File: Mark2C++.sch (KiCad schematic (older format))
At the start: 267 parts, among them U1 12AX7, U10 L7812, U11 6P6S, U15 6P6S, U2 12AX7, U3 12AX7, U4 NE5532, U5 NE5532, U6 NE5532, U7 NE5532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

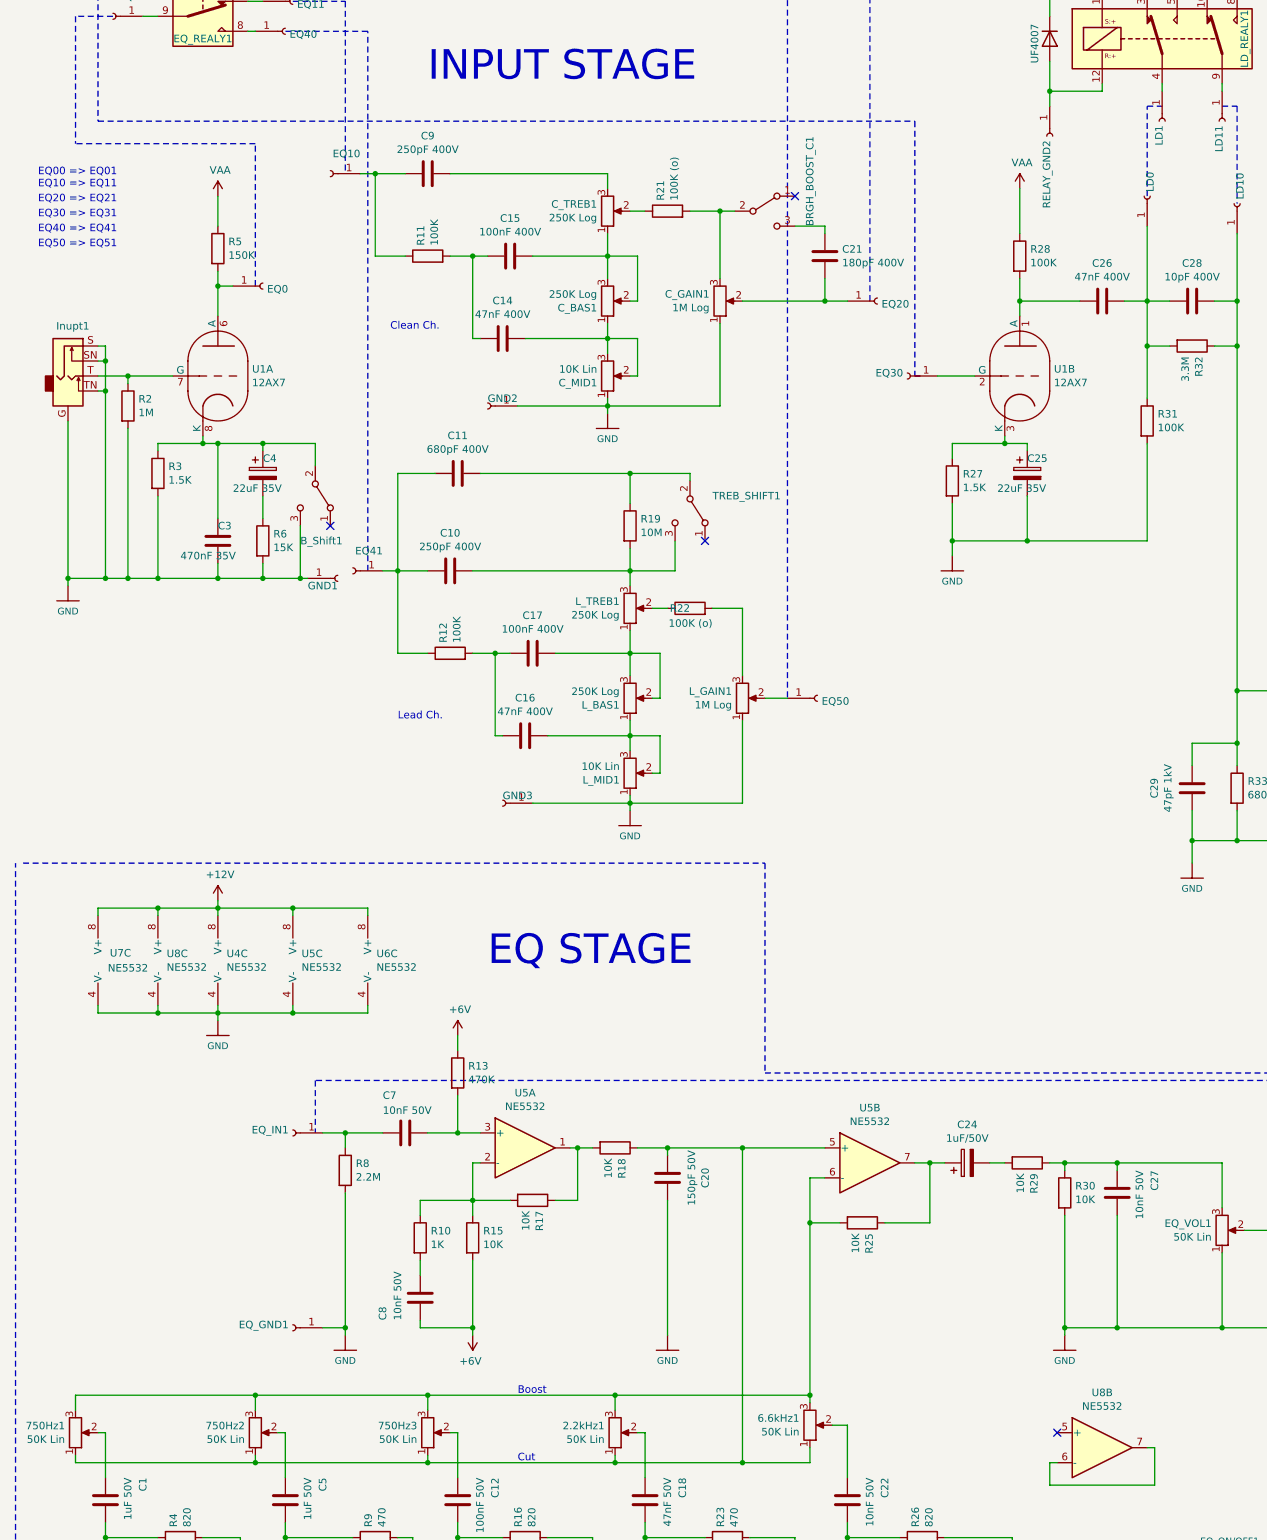
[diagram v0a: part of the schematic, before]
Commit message: small changes
- Poprawki w okolicach sekcji Lead
- Poprawiona nazwa wartości post EQ
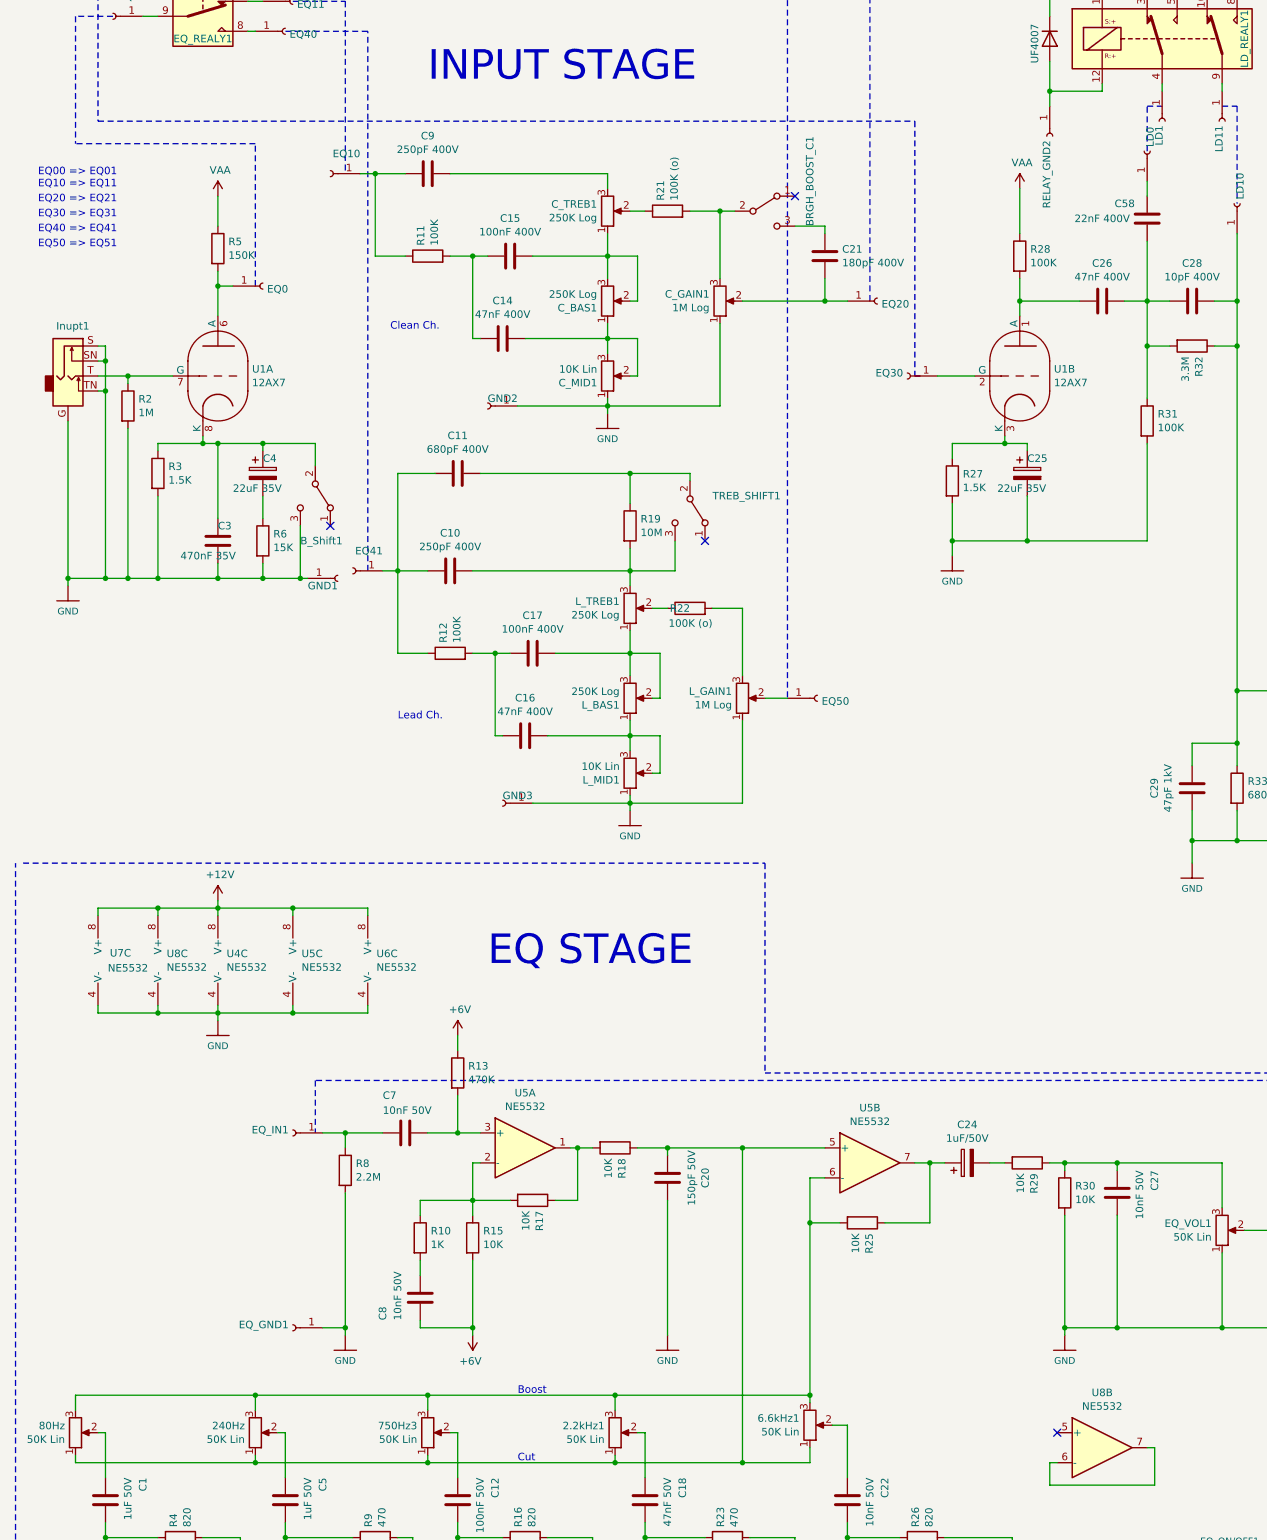
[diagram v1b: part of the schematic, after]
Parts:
- added C58: 22nF 400V, Capacitor_THT:C_Rect_L18.0mm_W6.0mm_P15.00mm_FKS3_FKP3, symbol Device:C
- renumbered 750Hz2 to 240Hz, 750Hz1 to 80Hz
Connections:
- net at C26.1, C28.2, R31.1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: now also C58.2; no longer LD0.1 (Pin_1)
- new net: C58.1, LD0.1 (Pin_1)
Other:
- moved on the sheet: LD0
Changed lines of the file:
@@
 L Connector:Conn_01x01_Female LD0
 U 1 1 64B6227D
-P 8000 3200
-F 0 "LD0" H 8028 3180 50  0000 L CNN
-F 1 "Conn_01x01_Female" H 8028 3135 50  0001 L CNN
-F 2 "Connectors:1X01_2MM" H 8000 3200 50  0001 C CNN
-F 3 "~" H 8000 3200 50  0001 C CNN
-	1    8000 3200
+P 8000 2900
+F 0 "LD0" H 8028 2880 50  0000 L CNN
+F 1 "Conn_01x01_Female" H 8028 2835 50  0001 L CNN
+F 2 "Connectors:1X01_2MM" H 8000 2900 50  0001 C CNN
+F 3 "~" H 8000 2900 50  0001 C CNN
+	1    8000 2900
 	0    -1   -1   0
 $EndComp
 Wire Wire Line
 	7850 3900 8000 3900
-Wire Wire Line
-	8000 3900 8000 3400
 $Comp
 L Device:C C28
@@
 	0    1    1    0
 $EndComp
-Wire Wire Line
-	8150 3900 8000 3900
 Connection ~ 8000 3900
 $Comp
@@
 	8500 2500 8500 2450
 Wire Notes Line rgb(255, 0, 0)
-	8000 3200 8000 2600
-Wire Notes Line rgb(255, 0, 0)
 	8000 2600 8100 2600
 Wire Notes Line rgb(255, 0, 0)
@@
 Connection ~ 2250 12150
 $Comp
-L Device:R_POT 750Hz2
+L Device:R_POT 240Hz
 U 1 1 65F391A3
 P 2050 11450
-F 0 "750Hz2" H 1980 11404 50  0000 R CNN
+F 0 "240Hz" H 1980 11404 50  0000 R CNN
 F 1 "50K Lin" H 1980 11495 50  0000 R CNN
 F 2 "Potentiometer_THT:Potentiometer_Bourns_PTA4543_Single_Slide" H 2050 11450 50  0001 C CNN
@@
 Connection ~ 1050 12850
 $Comp
-L Device:R_POT 750Hz1
+L Device:R_POT 80Hz
 U 1 1 663D8493
 P 850 11450
-F 0 "750Hz1" H 780 11404 50  0000 R CNN
+F 0 "80Hz" H 780 11404 50  0000 R CNN
 F 1 "50K Lin" H 780 11495 50  0000 R CNN
 F 2 "Potentiometer_THT:Potentiometer_Bourns_PTA4543_Single_Slide" H 850 11450 50  0001 C CNN
@@
 	1000 8650 1400 8650
 Connection ~ 1400 8650
+$Comp
+L Device:C C58
+U 1 1 64E58630
+P 8000 3350
+F 0 "C58" H 7850 3450 50  0000 C CNN
+F 1 "22nF 400V" H 7700 3350 50  0000 C CNN
+F 2 "Capacitor_THT:C_Rect_L18.0mm_W6.0mm_P15.00mm_FKS3_FKP3" H 8038 3200 50  0001 C CNN
+F 3 "~" H 8000 3350 50  0001 C CNN
+	1    8000 3350
+	1    0    0    -1
+$EndComp
+Wire Wire Line
+	8000 3200 8000 3100
+Wire Wire Line
+	8000 3500 8000 3900
+Wire Notes Line rgb(255, 0, 0)
+	8000 2900 8000 2600
+Wire Wire Line
+	8150 3900 8000 3900
 $EndSCHEMATC
